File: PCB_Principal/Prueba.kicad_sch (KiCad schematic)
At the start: 7 parts, among them Q811 BC807

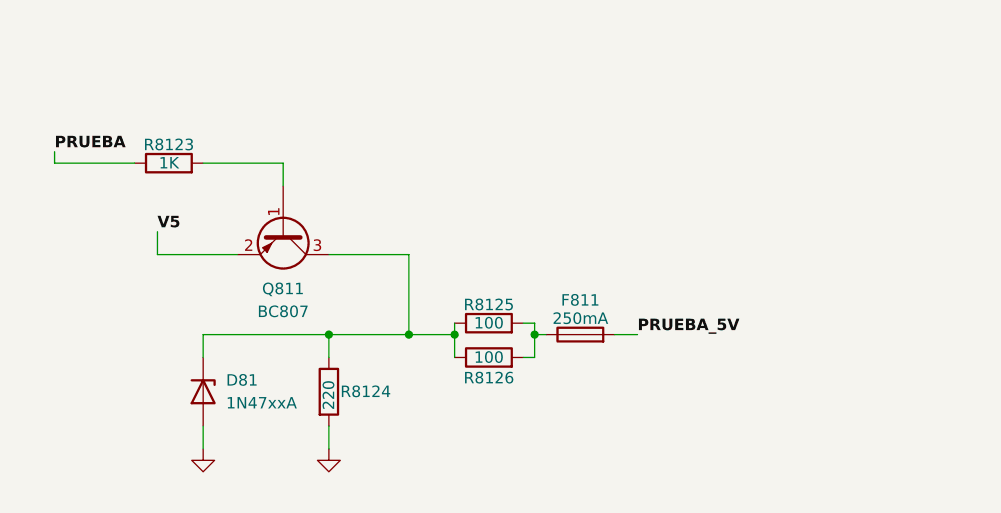
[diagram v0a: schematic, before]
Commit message: Versión 2 de esquemático, por GC.
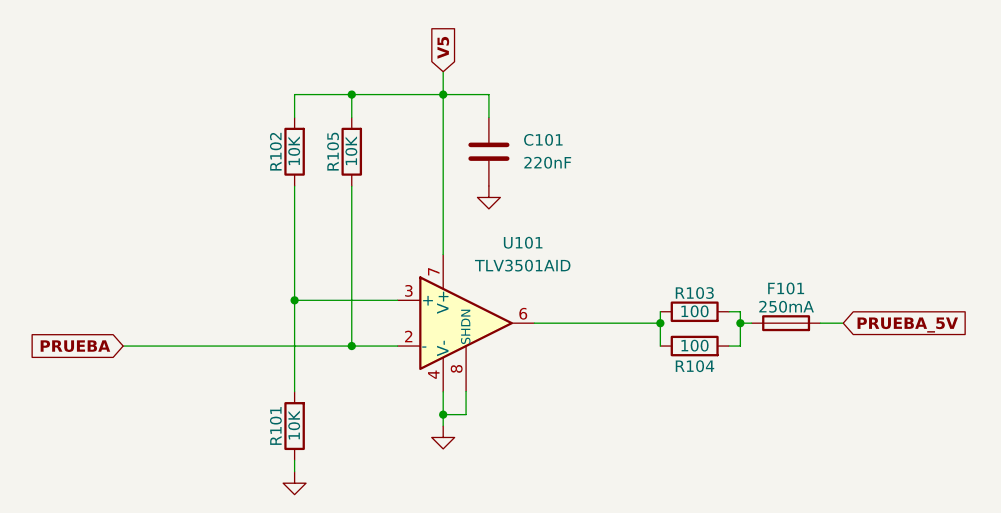
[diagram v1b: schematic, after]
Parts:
- removed D81: 1N47xxA, Diode_THT:D_DO-41_SOD81_P10.16mm_Horizontal, symbol Diode:1N47xxA
- removed Q811: BC807, Package_TO_SOT_SMD:SOT-23, symbol Transistor_BJT:BC807
- removed R8123: 1K, symbol Device:R
- removed R8124: 220, symbol Device:R
- added C101: 220nF, Capacitor_SMD:C_1206_3216Metric_Pad1.33x1.80mm_HandSolder, symbol Device:C
- added R101, R102, R105: 10K, Resistor_SMD:R_1206_3216Metric_Pad1.30x1.75mm_HandSolder, symbol Device:R
- added U101: TLV3501AID, Package_SO:SOIC-8_3.9x4.9mm_P1.27mm, symbol Comparator:TLV3501AID
- F101: renamed from F811; footprint (none) -> Fuse:Fuse_1812_4532Metric_Pad1.30x3.40mm_HandSolder
- R103: renamed from R8125; footprint (none) -> Resistor_SMD:R_1206_3216Metric_Pad1.30x1.75mm_HandSolder
- R104: renamed from R8126; footprint (none) -> Resistor_SMD:R_1206_3216Metric_Pad1.30x1.75mm_HandSolder
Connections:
- net GND: now also C101.1, R101.1, U101.4 (V-), U101.8 (SHDN)
- net PRUEBA: now also R105.1, U101.2 (-)
- net V5: now also C101.2, R102.2, R105.2, U101.7 (V+)
- net at R103.1, R104.1: now also U101.6
- new net: R101.2, R102.1, U101.3 (+)
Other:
- title: (none) -> Señal de prueba (ISPEL Beta 2024)
- moved on the sheet: F101, R103, R104

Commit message: Iniciando PCB...
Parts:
- renumbered C101 to C301, F101 to F301, R102 to R301, R101 to R302, R105 to R303, R103 to R304, R104 to R305, U101 to U301
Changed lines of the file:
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@@
 		(on_board yes)
 		(dnp no)
-		(property "Reference" "R103"
+		(property "Reference" "R304"
 			(at 179.07 93.218 90)
 			(effects
@@
 			(project "LabUNDAVGuillermo"
 				(path "/f66f0001-c0b9-4d2c-a26f-f2bac9dfd594/628bb6be-caa2-411c-826f-32d9289a60ba"
-					(reference "R103")
+					(reference "R304")
 					(unit 1)
 				)
@@
 		(on_board yes)
 		(dnp no)
-		(property "Reference" "R102"
+		(property "Reference" "R301"
 			(at 132.588 77.47 90)
 			(effects
@@
 			(project "ISPEL-CAD_v1"
 				(path "/f66f0001-c0b9-4d2c-a26f-f2bac9dfd594/628bb6be-caa2-411c-826f-32d9289a60ba"
-					(reference "R102")
+					(reference "R301")
 					(unit 1)
 				)
@@
 		(on_board yes)
 		(dnp no)
-		(property "Reference" "R104"
+		(property "Reference" "R305"
 			(at 179.07 101.346 90)
 			(effects
@@
 			(project "LabUNDAVGuillermo"
 				(path "/f66f0001-c0b9-4d2c-a26f-f2bac9dfd594/628bb6be-caa2-411c-826f-32d9289a60ba"
-					(reference "R104")
+					(reference "R305")
 					(unit 1)
 				)
@@
 		(dnp no)
 		(fields_autoplaced yes)
-		(property "Reference" "C101"
+		(property "Reference" "C301"
 			(at 160.02 76.1999 0)
 			(effects
@@
 			(project ""
 				(path "/f66f0001-c0b9-4d2c-a26f-f2bac9dfd594/628bb6be-caa2-411c-826f-32d9289a60ba"
-					(reference "C101")
+					(reference "C301")
 					(unit 1)
 				)
@@
 		(dnp no)
 		(fields_autoplaced yes)
-		(property "Reference" "#PWR0101"
+		(property "Reference" "#PWR0302"
 			(at 151.13 114.3 0)
 			(effects
@@
 			(project "LabUNDAVGuillermo"
 				(path "/f66f0001-c0b9-4d2c-a26f-f2bac9dfd594/628bb6be-caa2-411c-826f-32d9289a60ba"
-					(reference "#PWR0101")
+					(reference "#PWR0302")
 					(unit 1)
 				)
@@
 		(on_board yes)
 		(dnp no)
-		(property "Reference" "R101"
+		(property "Reference" "R302"
 			(at 132.588 107.95 90)
 			(effects
@@
 			(project "ISPEL-CAD_v1"
 				(path "/f66f0001-c0b9-4d2c-a26f-f2bac9dfd594/628bb6be-caa2-411c-826f-32d9289a60ba"
-					(reference "R101")
+					(reference "R302")
 					(unit 1)
 				)
@@
 		(on_board yes)
 		(dnp no)
-		(property "Reference" "U101"
+		(property "Reference" "U301"
 			(at 160.02 87.63 0)
 			(effects
@@
 			(project ""
 				(path "/f66f0001-c0b9-4d2c-a26f-f2bac9dfd594/628bb6be-caa2-411c-826f-32d9289a60ba"
-					(reference "U101")
+					(reference "U301")
 					(unit 1)
 				)
@@
 		(on_board yes)
 		(dnp no)
-		(property "Reference" "R105"
+		(property "Reference" "R303"
 			(at 138.938 77.47 90)
 			(effects
@@
 			(project "ISPEL-CAD_v1"
 				(path "/f66f0001-c0b9-4d2c-a26f-f2bac9dfd594/628bb6be-caa2-411c-826f-32d9289a60ba"
-					(reference "R105")
+					(reference "R303")
 					(unit 1)
 				)
@@
 		(dnp no)
 		(fields_autoplaced yes)
-		(property "Reference" "#PWR0103"
+		(property "Reference" "#PWR0301"
 			(at 134.62 119.38 0)
 			(effects
@@
 			(project "ISPEL-CAD_v1"
 				(path "/f66f0001-c0b9-4d2c-a26f-f2bac9dfd594/628bb6be-caa2-411c-826f-32d9289a60ba"
-					(reference "#PWR0103")
+					(reference "#PWR0301")
 					(unit 1)
 				)
@@
 		(dnp no)
 		(fields_autoplaced yes)
-		(property "Reference" "#PWR0102"
+		(property "Reference" "#PWR0303"
 			(at 156.21 87.63 0)
 			(effects
@@
 			(project "ISPEL-CAD_v1"
 				(path "/f66f0001-c0b9-4d2c-a26f-f2bac9dfd594/628bb6be-caa2-411c-826f-32d9289a60ba"
-					(reference "#PWR0102")
+					(reference "#PWR0303")
 					(unit 1)
 				)
@@
 		(on_board yes)
 		(dnp no)
-		(property "Reference" "F101"
+		(property "Reference" "F301"
 			(at 189.23 92.71 90)
 			(effects
@@
 			(project "LabUNDAVGuillermo"
 				(path "/f66f0001-c0b9-4d2c-a26f-f2bac9dfd594/628bb6be-caa2-411c-826f-32d9289a60ba"
-					(reference "F101")
-					(unit 1)
-				)
+					(reference "F301")
+					(unit 1)
+				)

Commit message: PCB con huella de portafusibles 1808.
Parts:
- F301: footprint Fuse:Fuse_1812_4532Metric_Pad1.30x3.40mm_HandSolder -> Libreria_ISPEL:Fuseholder_1808_handsoldering
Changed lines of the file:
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@@
 			)
 		)
-		(property "Footprint" "Fuse:Fuse_1812_4532Metric_Pad1.30x3.40mm_HandSolder"
+		(property "Footprint" "Libreria_ISPEL:Fuseholder_1808_handsoldering"
 			(at 189.23 98.298 90)
 			(effects

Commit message: Revisión 1. Con prototipo ISPEL Beta 2024 en fase de prueba.
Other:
- title: Señal de prueba (ISPEL Beta 2024) -> Señal de prueba (ISPEL Beta)
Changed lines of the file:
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@@
 	(paper "A4")
 	(title_block
-		(title "Señal de prueba (ISPEL Beta 2024)")
-		(date "2024-10-29")
-		(rev "2 (GC)")
+		(title "Señal de prueba (ISPEL Beta)")
+		(date "2025-04-04")
+		(rev "1")
 	)
 	(junction
